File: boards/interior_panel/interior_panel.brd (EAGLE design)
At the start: 99.1 x 71.1 mm, 28 parts, among them IC1 LM2576, IC2 DS1307, J1 POWER_JACKPTH_BREAD, Q1 MOSFET-NCHANNELFQP30N06L, U1 ATMEGA328P, U2 EXT ENCLOSURE, U3 DISPLAY, Y1 16MHz, Y2 32.786kHz

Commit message: PCB Update
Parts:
- C5: device nerdvellous-capacitors:CPOL-RADIAL-1000UF-25V -> nerdvellous-capacitors:CPOL-RADIAL-100UF-25V
- moved C5 1.27 mm to (38.7, 24.1)
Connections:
- net 5V: now also C5.1; no longer C5.+
- net GND: now also C5.2; no longer C5.-
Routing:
- net GND: track 386.0 -> 388.6 mm
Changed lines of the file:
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@@
 <setting verticaltext="up"/>
 </settings>
-<grid distance="0.025" unitdist="inch" unit="inch" style="lines" multiple="1" display="yes" altdistance="0.005" altunitdist="inch" altunit="inch"/>
+<grid distance="0.0125" unitdist="inch" unit="inch" style="lines" multiple="1" display="yes" altdistance="0.005" altunitdist="inch" altunit="inch"/>
 <layers>
 <layer number="1" name="Top" color="4" fill="1" visible="yes" active="yes"/>
@@
 <attribute name="PROD_ID_SF" value="CAP-08370" x="85.725" y="55.88" size="1.778" layer="27" display="off"/>
 </element>
-<element name="C5" library="nerdvellous-capacitors" package="CPOL-RADIAL-1000UF-25V" value="1000uF" x="38.735" y="22.86" rot="R90"/>
+<element name="C5" library="nerdvellous-capacitors" package="CPOL-RADIAL-100UF-25V" value="1000uF" x="38.735" y="24.13" rot="R90"/>
 <element name="C6" library="nerdvellous-capacitors" package="CAP-PTH-SMALL" value="0.1uF" x="82.55" y="24.765" rot="R270">
 <attribute name="PROD_ID_SF" value="CAP-08370" x="82.55" y="24.765" size="1.778" layer="27" rot="R270" display="off"/>
@@
 <contactref element="IC1" pad="P$3"/>
 <contactref element="IC1" pad="P$5"/>
-<contactref element="C5" pad="-"/>
+<contactref element="C5" pad="2"/>
 <contactref element="D1" pad="A"/>
 <contactref element="C1" pad="2"/>
@@
 <wire x1="52.705" y1="13.335" x2="50.165" y2="13.335" width="0.4064" layer="16"/>
 <wire x1="50.165" y1="13.335" x2="38.735" y2="13.335" width="0.4064" layer="16"/>
-<wire x1="23.495" y1="12.065" x2="24.765" y2="13.335" width="0.4064" layer="16"/>
-<wire x1="24.765" y1="13.335" x2="26.035" y2="12.065" width="0.4064" layer="16"/>
-<wire x1="26.035" y1="12.065" x2="27.305" y2="12.065" width="0.4064" layer="16"/>
-<wire x1="27.305" y1="12.065" x2="27.94" y2="12.7" width="0.4064" layer="16"/>
-<wire x1="27.94" y1="12.7" x2="27.94" y2="14.3256" width="0.4064" layer="16"/>
-<wire x1="27.94" y1="14.3256" x2="27.6606" y2="14.605" width="0.4064" layer="16"/>
-<wire x1="24.765" y1="14.605" x2="24.765" y2="13.335" width="0.4064" layer="16"/>
 <wire x1="12.065" y1="33.02" x2="9.525" y2="33.02" width="0.4064" layer="16"/>
 <wire x1="9.525" y1="33.02" x2="8.89" y2="32.385" width="0.4064" layer="16"/>
@@
 <wire x1="8.89" y1="26.035" x2="10.16" y2="24.765" width="0.4064" layer="16"/>
 <wire x1="10.16" y1="24.765" x2="15.875" y2="24.765" width="0.4064" layer="16"/>
-<wire x1="38.735" y1="20.32" x2="38.735" y2="13.335" width="0.4064" layer="16"/>
-<wire x1="38.735" y1="13.335" x2="28.9306" y2="13.335" width="0.4064" layer="16"/>
-<wire x1="28.9306" y1="13.335" x2="27.6606" y2="14.605" width="0.4064" layer="16"/>
+<wire x1="38.735" y1="22.86" x2="38.735" y2="13.335" width="0.4064" layer="16"/>
 <wire x1="53.34" y1="6.985" x2="53.975" y2="7.62" width="0.4064" layer="16"/>
 <wire x1="53.975" y1="7.62" x2="53.975" y2="10.795" width="0.4064" layer="16"/>
-<wire x1="23.495" y1="12.065" x2="16.96" y2="12.065" width="0.4064" layer="16"/>
-<wire x1="16.96" y1="12.065" x2="15.595" y2="10.7" width="0.4064" layer="16"/>
 <wire x1="10.795" y1="7.9" x2="9.245" y2="7.9" width="0.4064" layer="16"/>
 <wire x1="9.245" y1="7.9" x2="7.62" y2="9.525" width="0.4064" layer="16"/>
@@
 <wire x1="80.645" y1="69.215" x2="38.1" y2="69.215" width="0.4064" layer="16"/>
 <wire x1="38.1" y1="69.215" x2="36.195" y2="67.945" width="0.4064" layer="16"/>
-<wire x1="10.795" y1="7.9" x2="15.595" y2="10.7" width="0" layer="19" extent="1-1"/>
 <wire x1="34.925" y1="48.895" x2="36.83" y2="46.99" width="0.4064" layer="16"/>
 <wire x1="36.83" y1="46.99" x2="36.83" y2="46.355" width="0.4064" layer="16"/>
+<wire x1="38.735" y1="13.335" x2="29.9306" y2="13.335" width="0.4064" layer="16"/>
+<wire x1="29.9306" y1="13.335" x2="28.6606" y2="14.605" width="0.4064" layer="16"/>
+<wire x1="25.265" y1="14.605" x2="25.265" y2="12.835" width="0.4064" layer="16"/>
+<wire x1="25.265" y1="12.835" x2="26.035" y2="12.065" width="0.4064" layer="16"/>
+<wire x1="26.035" y1="12.065" x2="27.94" y2="12.065" width="0.4064" layer="16"/>
+<wire x1="27.94" y1="12.065" x2="28.575" y2="12.7" width="0.4064" layer="16"/>
+<wire x1="28.575" y1="12.7" x2="28.575" y2="14.5194" width="0.4064" layer="16"/>
+<wire x1="28.575" y1="14.5194" x2="28.6606" y2="14.605" width="0.4064" layer="16"/>
+<wire x1="15.595" y1="10.7" x2="24.67" y2="10.7" width="0.4064" layer="16"/>
+<wire x1="24.67" y1="10.7" x2="26.035" y2="12.065" width="0.4064" layer="16"/>
+<wire x1="10.795" y1="7.9" x2="15.595" y2="10.7" width="0" layer="19" extent="1-1"/>
 </signal>
 <signal name="N$1">
@@
 <wire x1="22.2631" y1="19.6469" x2="23.495" y2="18.415" width="0.4064" layer="16"/>
 <wire x1="23.495" y1="18.415" x2="23.495" y2="14.7828" width="0.4064" layer="16"/>
-<wire x1="23.495" y1="14.7828" x2="23.3172" y2="14.605" width="0.4064" layer="16"/>
+<wire x1="23.495" y1="14.7828" x2="23.6172" y2="14.605" width="0.4064" layer="16"/>
 <wire x1="27.305" y1="33.02" x2="31.115" y2="33.02" width="0.4064" layer="16"/>
 <wire x1="31.115" y1="33.02" x2="32.385" y2="31.75" width="0.4064" layer="16"/>
@@
 <contactref element="L1" pad="2"/>
 <contactref element="IC1" pad="P$4"/>
-<contactref element="C5" pad="+"/>
+<contactref element="C5" pad="1"/>
 <contactref element="R1" pad="P$1"/>
 <contactref element="U1" pad="20"/>
@@
 <contactref element="C2" pad="1"/>
 <contactref element="U$1" pad="VCC"/>
-<wire x1="27.2669" y1="23.495" x2="27.2669" y2="19.6469" width="0.4064" layer="16"/>
-<wire x1="27.2669" y1="19.6469" x2="26.035" y2="18.415" width="0.4064" layer="16"/>
-<wire x1="26.035" y1="18.415" x2="26.035" y2="14.7828" width="0.4064" layer="16"/>
-<wire x1="26.035" y1="14.7828" x2="26.2128" y2="14.605" width="0.4064" layer="16"/>
 <wire x1="38.735" y1="25.4" x2="29.1719" y2="25.4" width="0.4064" layer="16"/>
 <wire x1="29.1719" y1="25.4" x2="27.2669" y2="23.495" width="0.4064" layer="16"/>
@@
 <wire x1="75.565" y1="38.1" x2="70.993" y2="42.672" width="0.4064" layer="16"/>
 <wire x1="70.993" y1="42.672" x2="70.993" y2="43.815" width="0.4064" layer="16"/>
+<wire x1="26.9128" y1="14.605" x2="26.9875" y2="14.605" width="0.4064" layer="16"/>
+<wire x1="26.9875" y1="14.605" x2="26.9875" y2="22.8981" width="0.4064" layer="16"/>
+<wire x1="26.9875" y1="22.8981" x2="27.2669" y2="23.495" width="0.4064" layer="16"/>
 </signal>
 <signal name="CMD_DOOR">
@@
 <contactref element="U2" pad="5"/>
 <contactref element="U1" pad="17"/>
-<wire x1="41.275" y1="66.675" x2="41.91" y2="66.675" width="0.4064" layer="16"/>
-<wire x1="41.91" y1="66.675" x2="48.895" y2="59.69" width="0.4064" layer="16"/>
-<wire x1="48.895" y1="59.69" x2="59.055" y2="59.69" width="0.4064" layer="16"/>
+<wire x1="41.275" y1="66.675" x2="48.26" y2="59.69" width="0.4064" layer="16"/>
+<wire x1="48.26" y1="59.69" x2="59.055" y2="59.69" width="0.4064" layer="16"/>
 </signal>
 <signal name="N$19">

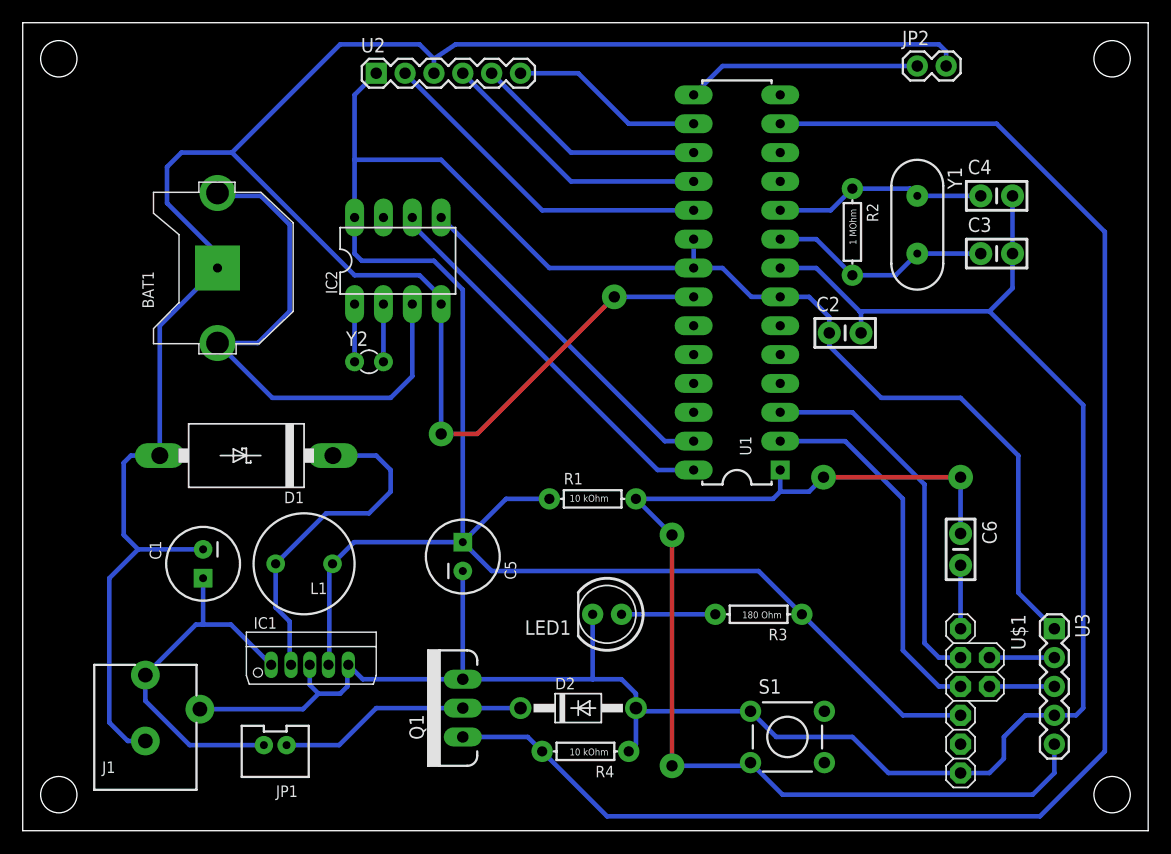
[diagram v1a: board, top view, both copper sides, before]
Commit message: Bigger power track (5V, 12V, and GND)
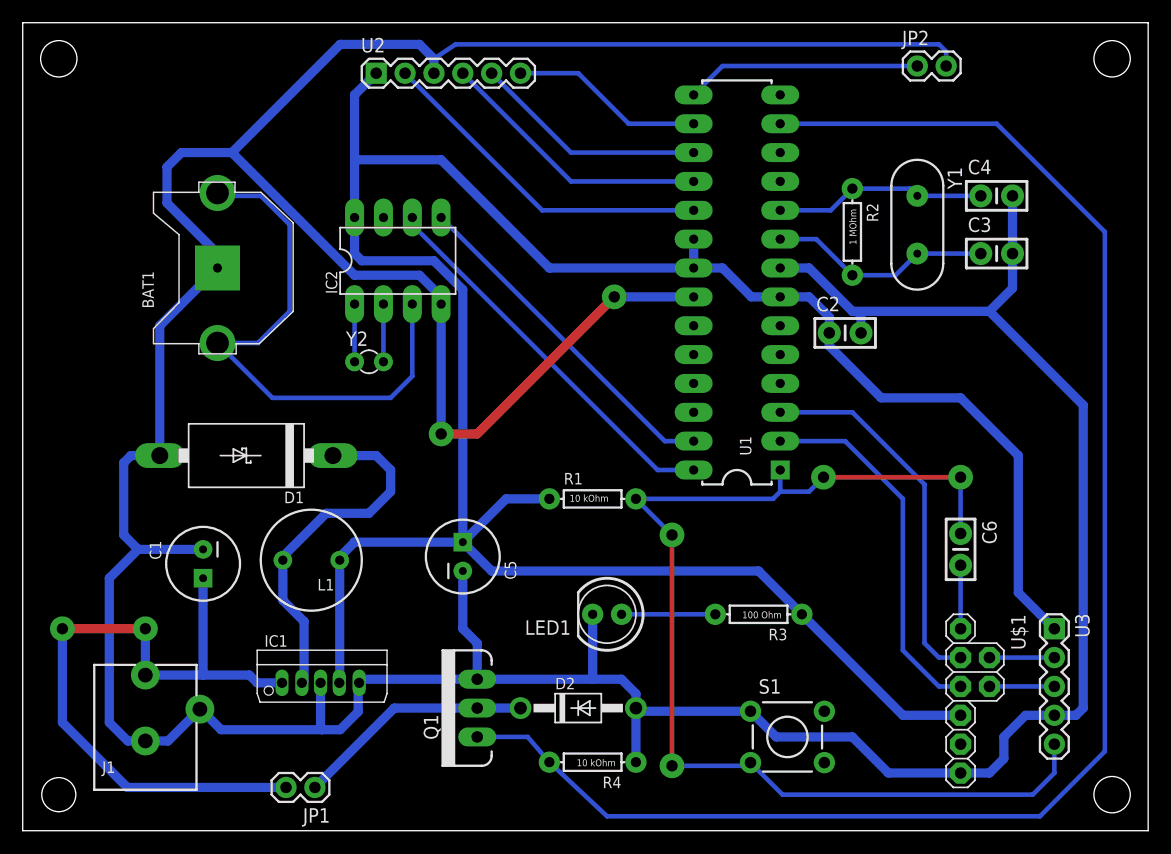
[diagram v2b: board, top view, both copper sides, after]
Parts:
- JP1: value M02JST-PTH-VERT -> M02PTH; device nerdvellous-connectors:JST-2-PTH-VERT -> nerdvellous-connectors:1X02
- R3: value 180 Ohm -> 100 Ohm
- moved JP1 4.72 mm to (25.7, 3.81)
- moved IC1 1.85 mm to (25.7, 13.0)
- moved Q1 1.27 mm to (40.0, 10.8)
- moved R4 1.14 mm to (50.2, 6.03)
- moved L1 0.71 mm to (25.4, 23.8)
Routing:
- net 12V: track 32.8 -> 62.5 mm, vias 0 -> 2
- net GND: track 388.6 -> 398.5 mm
- net N$1: track 29.7 -> 31.3 mm
- net CMD_DOOR: track 140.0 -> 138.8 mm
- net 5V: track 220.1 -> 221.3 mm
- net N$3: track 21.9 -> 21.0 mm
